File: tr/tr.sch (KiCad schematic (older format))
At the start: 25 parts

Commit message: work on t/r schematic
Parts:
- added C10, C8: .022uF, ~, symbol C
- added C4: 22uF, ~, symbol CAPAPOL
- added C9: .02uF, ~, symbol C
- added D1, D6: 1N4001, ~, symbol DIODE
- added K1: CONN_3, ~, symbol CONN_3
- added L1, L6: 22uH, ~, symbol INDUCTOR
- added Q1: 2N2222A, ~, symbol NPN
- added Q2: NPN, ~, symbol NPN
- added R1: 10k, ~, symbol R
- added R10, R11: 150, ~, symbol R
- added R12: 220, ~, symbol R
- added R13, R2: 1k, ~, symbol R
- added R3: 510, ~, symbol R
- added R6: 200, ~, symbol R
- added R7: 22, ~, symbol R
- added R8, R9: 0, ~, symbol R
- C11, C2, C6: renamed from C?; value C -> .022uF
- C3: renamed from C?; value C -> .01uF 100V
- C7: renamed from C?; value C -> .05uF
- D7, D8: renamed from D?; value DIODE -> 1N4001
- L2, L3, L4, L5: renamed from L?; value INDUCTOR -> 22uH
- gave numbers to parts that had none: 14
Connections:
- net labels added: E1, E2
- net labels removed: TR_HV
- wire segments 68 -> 111
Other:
- note added: "22uH - SRR7032-220MCT-ND"
- note added: "ANT"
- note added: "RX"
- note added: "SRN3015-220MCT-ND"
- note added: "TX"
- moved on the sheet: C1, C11, C2, C3, C5, C6, C7, D2, D3, D4, D5, D7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

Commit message: more work on t/r schematic, almost done?
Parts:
- removed C10, C8: .022uF, ~, symbol C
- removed C4: 22uF, ~, symbol CAPAPOL
- removed L3: 22uH, ~, symbol INDUCTOR
- removed Q1: 2N2222A, ~, symbol NPN
- removed Q2: NPN, ~, symbol NPN
- removed R1: 10k, ~, symbol R
- removed R12: 220, ~, symbol R
- removed R3: 510, ~, symbol R
- removed R6: 200, ~, symbol R
- removed R7: 22, ~, symbol R
- added C?: .022uF, 1210, symbol C
- added C? (x2): 10nF, ~, symbol C
- added C? (x2): C, ~, symbol C
- added C? (x2): 10nF, 0805, symbol C
- added C? (x4): 100pF, 0805, symbol C
- added C?: .022uF 100V, ~, symbol C
- added L?: 22uH, ~, symbol INDUCTOR
- added R? (x2): 500, 0805, symbol R
- added R? (x4): 10k, ~, symbol R
- added R? (x4): 20k, ~, symbol R
- added R?: 400, 0805, symbol R
- added R? (x4): 22, 0805, symbol R
- added U?: LT1631, ~, symbol LT1631
- C1: value C -> 100nF; footprint ~ -> 0805
- C11, C2, C6: footprint ~ -> 1210
- C3: value .01uF 100V -> 10nF; footprint ~ -> 0805
- C5: value C -> 68nF; footprint ~ -> 0805
- C7: value .05uF -> .022uF; footprint ~ -> 1210
- C9: value .02uF -> .022uF; footprint ~ -> 1210
- D1, D6, D7, D8: value 1N4001 -> ES2A; footprint ~ -> SMB
- D2, D4: value DIODE -> MA4P4006F-1091T; footprint ~ -> MELF-1072
- D3, D5: value DIODE -> MA4P7006F-1072T; footprint ~ -> MELF-1072
- Q3, Q4: value MOSFET_N -> STD2NK90ZT4; footprint ~ -> TO-252-3
- R10, R13, R2, R8, R9: footprint ~ -> 0805
- R11: value 150 -> 500; footprint ~ -> 0805
- R4, R5: value R -> 1k; footprint ~ -> 0805
- U1: footprint (none) -> S0-8
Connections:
- net labels added: OUTA, OUTB, OUTC, OUTD, VEE
- wire segments 111 -> 155
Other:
- note added: ".022 uF 1210 C1210X223KFRACTU"
- note added: "20 mA on\n"
- note added: "20 mA on\n\n"
- note added: "22uH - SRN3015-220MCT-ND"
- note added: "40 mA on\n"
- note removed: "22uH - SRR7032-220MCT-ND"
- note removed: "SRN3015-220MCT-ND"
- moved on the sheet: J2, K1, R11

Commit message: more work on pin diode drivers
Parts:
- added C10: .022uF, 1210, symbol C
- added C?: 10uF, ~, symbol CAPAPOL
- added C?: 10nF, ~, symbol C
- added C?: 2.2uF, ~, symbol C
- added D10, D9: ES2A, SMB, symbol DIODE
- added R12, R14: 10k, ~, symbol R
- added R15: RVAR, ~, symbol RVAR
- added R? (x2): 20k, ~, symbol R
- C13, C4: renamed from C?; value C -> 2.2uF
- R11: value 500 -> 470
- R21: renamed from R?; value 400 -> 330
- R22, R25: renamed from R?; value 500 -> 470
- gave numbers to parts that had none: 24
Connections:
- net labels added: RX, TX
- net labels removed: E1, E2
- wire segments 155 -> 178
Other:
- moved on the sheet: C1, C11, C12, C13, C14, C15, C16, C17, C18, C19, C2, C20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

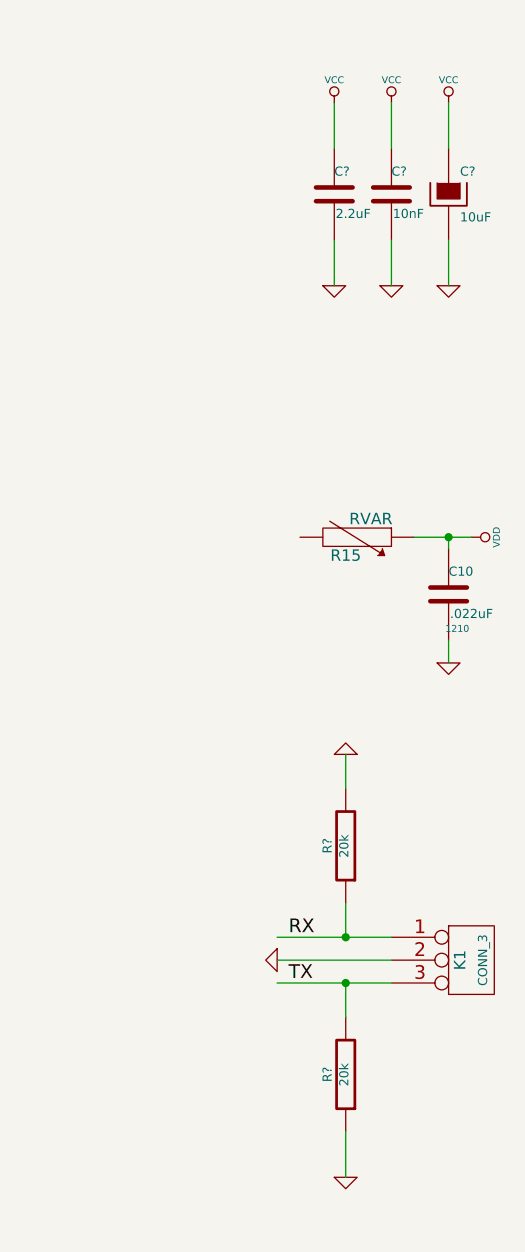
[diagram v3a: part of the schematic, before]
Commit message: created footprints and started board layout for tr
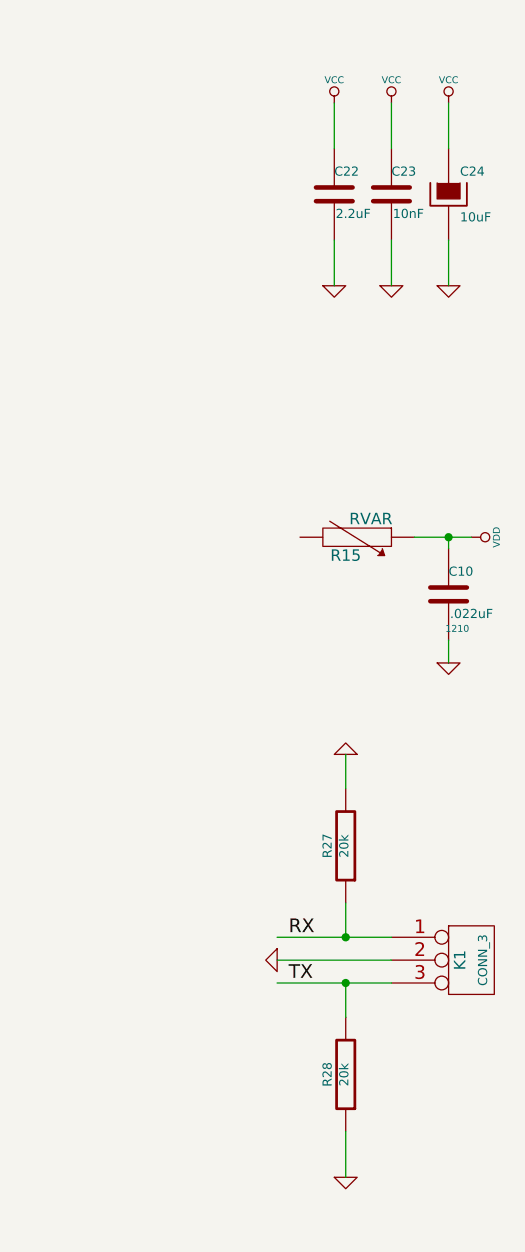
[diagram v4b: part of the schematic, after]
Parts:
- gave numbers to parts that had none: 5

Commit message: updated transmitter layout
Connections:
- net labels added: hv_vdd, hvbias, hvd, hvdiode, hvout, hvs
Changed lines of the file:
@@
 Sheet 1 1
 Title "High Power TX/RX Switch"
-Date "16 dec 2013"
+Date "17 dec 2013"
 Rev "0"
 Comp "Geophysical Institute, University of Alaska, Fairbanks"
@@
 Wire Wire Line
 	14000 3250 14000 3450
+Text Label 7600 7300 0    60   ~ 0
+hv_vdd
+Text Label 7600 7850 0    60   ~ 0
+hvs
+Text Label 7600 8400 0    60   ~ 0
+hvout
+Text Label 7600 8950 0    60   ~ 0
+hvd
+Text Label 8700 8400 0    60   ~ 0
+hvbias
+Text Label 8900 5650 0    60   ~ 0
+hvdiode
 $EndSCHEMATC

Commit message: added hv power supply, footprints
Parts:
- added C25, C27, C29, C31, C33: 47uF, ~, symbol CAPAPOL
- added C26: 100pF, 0805, symbol C
- added C28: 22nF, 0805, symbol C
- added C30: 100nF, 0805, symbol C
- added C32: 10nF, 0603, symbol C
- added C34: 220pF, 0805, symbol C
- added C35, C36: 68nF, 1210, symbol C
- added D11: GSD2004S, SOT-23, symbol DIODE
- added Q?: Si7850, ~, symbol MOS_N_PPAK
- added R29: 6.8k, 0805, symbol R
- added R30: 140k, 0805, symbol R
- added R31: 46.4k, 0603, symbol R
- added R32: 105k, 0603, symbol R
- added R33: 22, 0603, symbol R
- added R34: .02, 0805, symbol R
- added R35: 22, 0805, symbol R
- added R36: 1.5M, 0603, symbol R
- added R37, R38: 1M, 0603, symbol R
- added R39: 16.2k, 0603, symbol R
- added R40: 1M, 1210, symbol R
- added T?: DA2033-AL_, ~, symbol TRANSFO_MULTI
- added U3: LT3757, ~, symbol LT3757
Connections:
- wire segments 178 -> 255
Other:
- note added: "300V Power Supply\n"
- note added: "High Power HF T/R Switch"
- note added: "PIN Diode Current Driver"
- note added: "PIN Diode HV Bias"
- moved on the sheet: C1, C10, C11, C12, C13, C14, C15, C16, C17, C18, C19, C2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

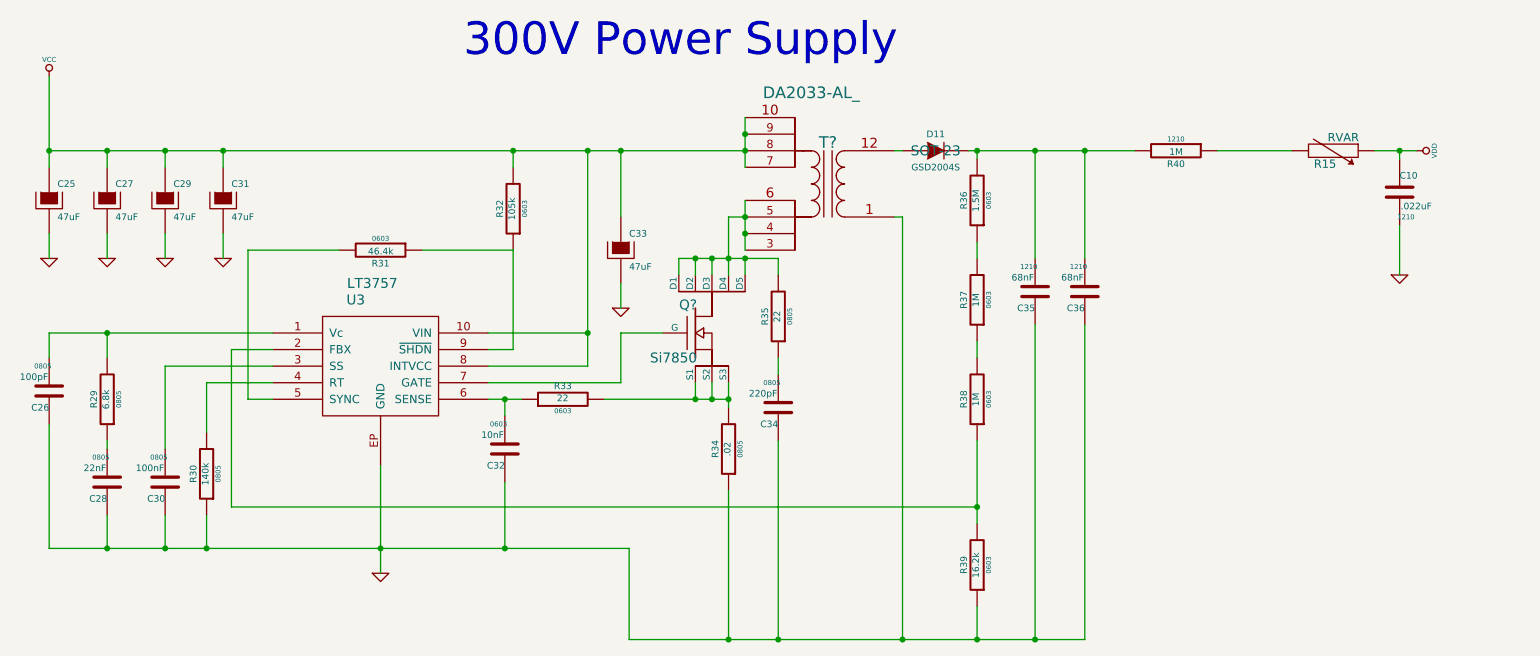
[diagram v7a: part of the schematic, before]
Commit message: component placement on hv power supply
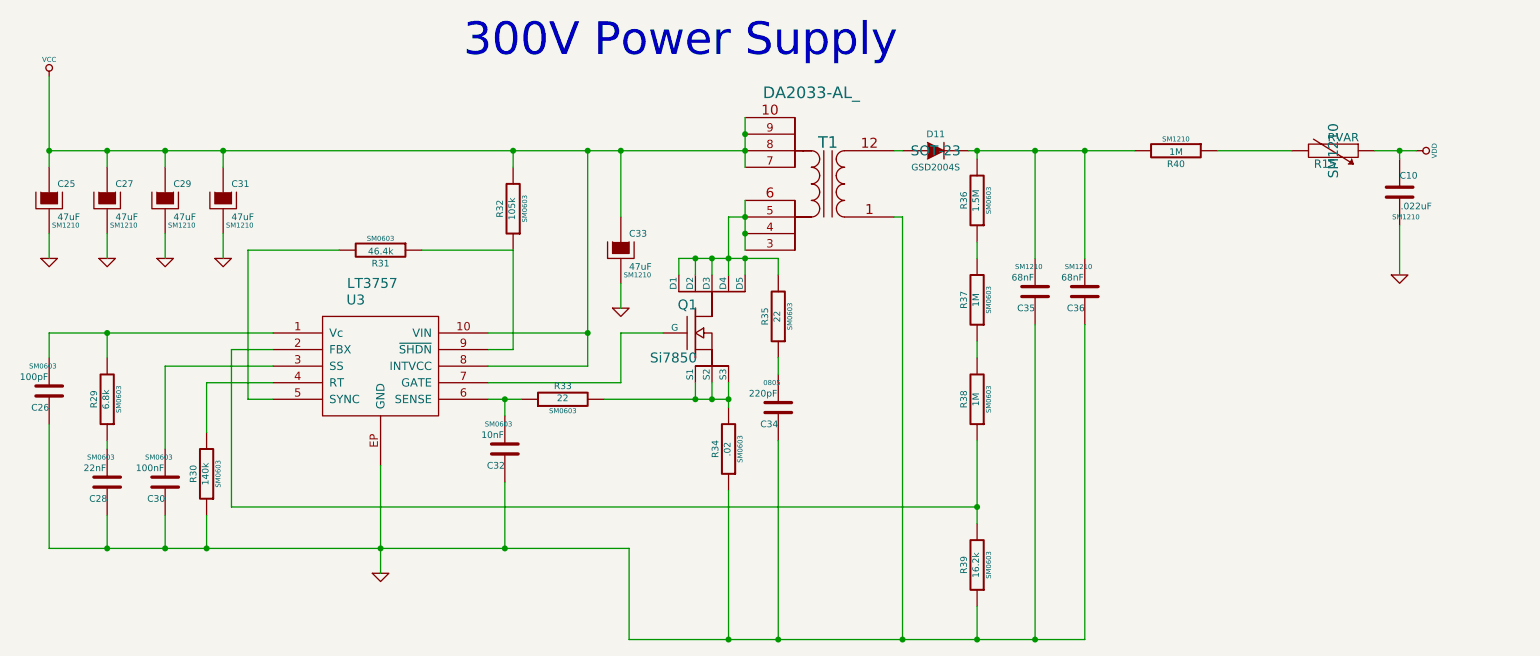
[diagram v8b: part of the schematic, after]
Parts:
- C10, C35, C36, R40: footprint 1210 -> SM1210
- C25, C27, C29, C31, C33, R15: footprint ~ -> SM1210
- C26, C28, C30, R29, R30, R34, R35: footprint 0805 -> SM0603
- C32, R31, R32, R33, R36, R37, R38, R39: footprint 0603 -> SM0603
- gave numbers to parts that had none: 2
